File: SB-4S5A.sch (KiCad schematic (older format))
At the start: 39 parts, among them J1 LEMO6, Q1 CSD17308Q3, Q2 CSD17308Q3, Q3 2N7002, U1 bq40z50-r2

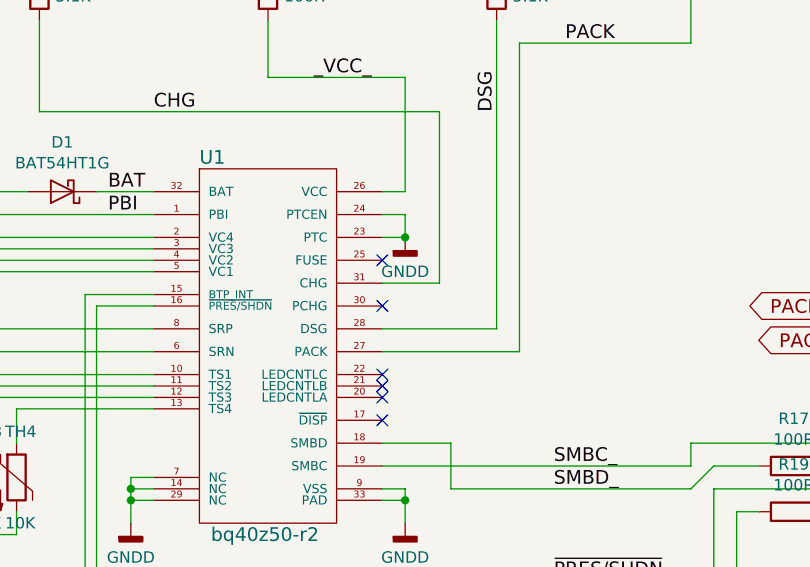
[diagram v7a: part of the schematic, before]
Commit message: Fix FUSE pin floating.
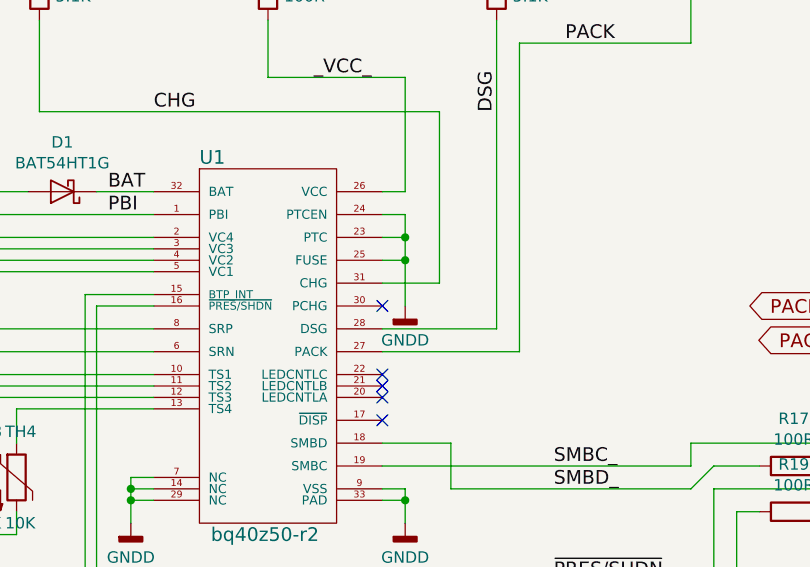
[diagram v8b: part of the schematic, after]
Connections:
- wire segments 187 -> 190
- no-connect marks 6 -> 5
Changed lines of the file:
@@
 	1    0    0    -1
 $EndComp
-NoConn ~ 6550 3500
 NoConn ~ 6550 3700
 $Comp
@@
 L power:GNDD #PWR06
 U 1 1 597D8A8D
-P 6650 3400
-F 0 "#PWR06" H 6650 3150 50  0001 C CNN
-F 1 "GNDD" H 6650 3250 50  0000 C CNN
-F 2 "" H 6650 3400 50  0001 C CNN
-F 3 "" H 6650 3400 50  0001 C CNN
-	1    6650 3400
+P 6650 3700
+F 0 "#PWR06" H 6650 3450 50  0001 C CNN
+F 1 "GNDD" H 6650 3550 50  0000 C CNN
+F 2 "" H 6650 3700 50  0001 C CNN
+F 3 "" H 6650 3700 50  0001 C CNN
+	1    6650 3700
 	1    0    0    -1
 $EndComp
@@
 	6550 4550 6650 4550
 Connection ~ 6650 4550
-Wire Wire Line
-	6550 3400 6650 3400
-Wire Wire Line
-	6650 3400 6650 3300
 Wire Wire Line
 	6650 3300 6550 3300
@@
 Text Label 7050 1950 1    60   ~ 0
 DSG_G
-Connection ~ 6650 3400
 $Comp
 L power:GNDD #PWR01
@@
 Wire Wire Line
 	8500 4600 10450 4600
+Wire Wire Line
+	6650 3300 6650 3400
+Wire Wire Line
+	6550 3400 6650 3400
+Connection ~ 6650 3400
+Wire Wire Line
+	6650 3400 6650 3500
+Wire Wire Line
+	6550 3500 6650 3500
+Connection ~ 6650 3500
+Wire Wire Line
+	6650 3500 6650 3700
 $EndSCHEMATC
